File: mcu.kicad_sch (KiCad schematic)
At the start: 30 parts, among them J1 10118193-0001LF, U1 RP2040, U2 AP2112K-3.3TRG1, U3 W25Q16JVSSIQ, Y3 12MHZ

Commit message: Use 402 footprint for rp2040 mcu part
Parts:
- C10, C12, C13, C14, C15, C17, C18, C19, C20, C21, C22, C23, C24, C25: footprint Capacitor_SMD:C_0603_1608Metric_Pad1.08x0.95mm_HandSolder -> Capacitor_SMD:C_0402_1005Metric
- R4, R5, R6, R7, R8, R9: footprint Resistor_SMD:R_0603_1608Metric_Pad0.98x0.95mm_HandSolder -> Resistor_SMD:R_0402_1005Metric
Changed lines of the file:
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@@
       (effects (font (size 1.27 1.27)) (justify left))
     )
-    (property "Footprint" "Capacitor_SMD:C_0603_1608Metric_Pad1.08x0.95mm_HandSolder" (at 187.6552 96.52 0)
+    (property "Footprint" "Capacitor_SMD:C_0402_1005Metric" (at 187.6552 96.52 0)
       (effects (font (size 1.27 1.27)) hide)
     )
@@
       (effects (font (size 1.27 1.27)) (justify left))
     )
-    (property "Footprint" "Capacitor_SMD:C_0603_1608Metric_Pad1.08x0.95mm_HandSolder" (at 221.9452 96.52 0)
+    (property "Footprint" "Capacitor_SMD:C_0402_1005Metric" (at 221.9452 96.52 0)
       (effects (font (size 1.27 1.27)) hide)
     )
@@
       (effects (font (size 1.27 1.27)) (justify left))
     )
-    (property "Footprint" "Capacitor_SMD:C_0603_1608Metric_Pad1.08x0.95mm_HandSolder" (at 275.2852 96.52 0)
+    (property "Footprint" "Capacitor_SMD:C_0402_1005Metric" (at 275.2852 96.52 0)
       (effects (font (size 1.27 1.27)) hide)
     )
@@
       (effects (font (size 1.27 1.27)))
     )
-    (property "Footprint" "Resistor_SMD:R_0603_1608Metric_Pad0.98x0.95mm_HandSolder" (at 198.12 125.222 90)
+    (property "Footprint" "Resistor_SMD:R_0402_1005Metric" (at 198.12 125.222 90)
       (effects (font (size 1.27 1.27)) hide)
     )
@@
       (effects (font (size 1.27 1.27)) (justify left))
     )
-    (property "Footprint" "Capacitor_SMD:C_0603_1608Metric_Pad1.08x0.95mm_HandSolder" (at 263.8552 96.52 0)
+    (property "Footprint" "Capacitor_SMD:C_0402_1005Metric" (at 263.8552 96.52 0)
       (effects (font (size 1.27 1.27)) hide)
     )
@@
       (effects (font (size 1.27 1.27)))
     )
-    (property "Footprint" "Resistor_SMD:R_0603_1608Metric_Pad0.98x0.95mm_HandSolder" (at 158.75 151.892 90)
+    (property "Footprint" "Resistor_SMD:R_0402_1005Metric" (at 158.75 151.892 90)
       (effects (font (size 1.27 1.27)) hide)
     )
@@
       (effects (font (size 1.27 1.27)) (justify left))
     )
-    (property "Footprint" "Capacitor_SMD:C_0603_1608Metric_Pad1.08x0.95mm_HandSolder" (at 199.0852 96.52 0)
+    (property "Footprint" "Capacitor_SMD:C_0402_1005Metric" (at 199.0852 96.52 0)
       (effects (font (size 1.27 1.27)) hide)
     )
@@
       (effects (font (size 1.27 1.27)) (justify left))
     )
-    (property "Footprint" "Capacitor_SMD:C_0603_1608Metric_Pad1.08x0.95mm_HandSolder" (at 168.6052 173.99 0)
+    (property "Footprint" "Capacitor_SMD:C_0402_1005Metric" (at 168.6052 173.99 0)
       (effects (font (size 1.27 1.27)) hide)
     )
@@
       (effects (font (size 1.27 1.27)) (justify left))
     )
-    (property "Footprint" "Capacitor_SMD:C_0603_1608Metric_Pad1.08x0.95mm_HandSolder" (at 150.8252 173.99 0)
+    (property "Footprint" "Capacitor_SMD:C_0402_1005Metric" (at 150.8252 173.99 0)
       (effects (font (size 1.27 1.27)) hide)
     )
@@
       (effects (font (size 1.27 1.27)) (justify left))
     )
-    (property "Footprint" "Capacitor_SMD:C_0603_1608Metric_Pad1.08x0.95mm_HandSolder" (at 154.6352 73.66 0)
+    (property "Footprint" "Capacitor_SMD:C_0402_1005Metric" (at 154.6352 73.66 0)
       (effects (font (size 1.27 1.27)) hide)
     )
@@
       (effects (font (size 1.27 1.27)) (justify left))
     )
-    (property "Footprint" "Capacitor_SMD:C_0603_1608Metric_Pad1.08x0.95mm_HandSolder" (at 244.8052 96.52 0)
+    (property "Footprint" "Capacitor_SMD:C_0402_1005Metric" (at 244.8052 96.52 0)
       (effects (font (size 1.27 1.27)) hide)
     )
@@
       (effects (font (size 1.27 1.27)))
     )
-    (property "Footprint" "Resistor_SMD:R_0603_1608Metric_Pad0.98x0.95mm_HandSolder" (at 128.27 132.842 90)
+    (property "Footprint" "Resistor_SMD:R_0402_1005Metric" (at 128.27 132.842 90)
       (effects (font (size 1.27 1.27)) hide)
     )
@@
       (effects (font (size 1.27 1.27)) (justify left))
     )
-    (property "Footprint" "Capacitor_SMD:C_0603_1608Metric_Pad1.08x0.95mm_HandSolder" (at 135.5852 162.56 0)
+    (property "Footprint" "Capacitor_SMD:C_0402_1005Metric" (at 135.5852 162.56 0)
       (effects (font (size 1.27 1.27)) hide)
     )
@@
       (effects (font (size 1.27 1.27)) (justify left))
     )
-    (property "Footprint" "Resistor_SMD:R_0603_1608Metric_Pad0.98x0.95mm_HandSolder" (at 165.862 160.02 90)
+    (property "Footprint" "Resistor_SMD:R_0402_1005Metric" (at 165.862 160.02 90)
       (effects (font (size 1.27 1.27)) hide)
     )
@@
       (effects (font (size 1.27 1.27)) (justify left))
     )
-    (property "Footprint" "Resistor_SMD:R_0603_1608Metric_Pad0.98x0.95mm_HandSolder" (at 202.692 120.65 90)
+    (property "Footprint" "Resistor_SMD:R_0402_1005Metric" (at 202.692 120.65 90)
       (effects (font (size 1.27 1.27)) hide)
     )
@@
       (effects (font (size 1.27 1.27)))
     )
-    (property "Footprint" "Resistor_SMD:R_0603_1608Metric_Pad0.98x0.95mm_HandSolder" (at 128.27 140.462 90)
+    (property "Footprint" "Resistor_SMD:R_0402_1005Metric" (at 128.27 140.462 90)
       (effects (font (size 1.27 1.27)) hide)
     )
@@
       (effects (font (size 1.27 1.27)) (justify left))
     )
-    (property "Footprint" "Capacitor_SMD:C_0603_1608Metric_Pad1.08x0.95mm_HandSolder" (at 125.4252 162.56 0)
+    (property "Footprint" "Capacitor_SMD:C_0402_1005Metric" (at 125.4252 162.56 0)
       (effects (font (size 1.27 1.27)) hide)
     )
@@
       (effects (font (size 1.27 1.27)) (justify left))
     )
-    (property "Footprint" "Capacitor_SMD:C_0603_1608Metric_Pad1.08x0.95mm_HandSolder" (at 176.2252 96.52 0)
+    (property "Footprint" "Capacitor_SMD:C_0402_1005Metric" (at 176.2252 96.52 0)
       (effects (font (size 1.27 1.27)) hide)
     )
@@
       (effects (font (size 1.27 1.27)) (justify left))
     )
-    (property "Footprint" "Capacitor_SMD:C_0603_1608Metric_Pad1.08x0.95mm_HandSolder" (at 210.5152 96.52 0)
+    (property "Footprint" "Capacitor_SMD:C_0402_1005Metric" (at 210.5152 96.52 0)
       (effects (font (size 1.27 1.27)) hide)
     )
@@
       (effects (font (size 1.27 1.27)) (justify left))
     )
-    (property "Footprint" "Capacitor_SMD:C_0603_1608Metric_Pad1.08x0.95mm_HandSolder" (at 233.3752 96.52 0)
-      (effects (font (size 1.27 1.27)) hide)
-    )
+    (property "Footprint" "Capacitor_SMD:C_0402_1005Metric" (at 233.3752 96.52 0)
+      (effects (font (size 1.27 1.27)) hide)
+    )

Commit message: Update design
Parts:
- C16: footprint Capacitor_SMD:C_0603_1608Metric_Pad1.08x0.95mm_HandSolder -> Capacitor_SMD:C_0402_1005Metric
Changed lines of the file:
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@@
       (effects (font (size 1.27 1.27)) (justify left))
     )
-    (property "Footprint" "Capacitor_SMD:C_0603_1608Metric_Pad1.08x0.95mm_HandSolder" (at 267.6652 134.62 0)
+    (property "Footprint" "Capacitor_SMD:C_0402_1005Metric" (at 267.6652 134.62 0)
       (effects (font (size 1.27 1.27)) hide)
     )

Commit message: Update design
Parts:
- added J5: Conn_ARM_SWD_TagConnect_TC2030, Connector:Tag-Connect_TC2030-IDC-NL_2x03_P1.27mm_Vertical, symbol Connector:Conn_ARM_SWD_TagConnect_TC2030
- added LED1: 150060VS75000, LED_SMD:LED_0603_1608Metric, symbol rpi-pico-debugger-shoe-rescue:150060VS75000-150060VS75000
- added R2: 1K, Resistor_SMD:R_0402_1005Metric, symbol Device:R
- added SW1: SW_Push, Button_Switch_SMD:SW_SPST_B3U-1000P, symbol Switch:SW_Push
- R1: footprint Resistor_SMD:R_0603_1608Metric_Pad0.98x0.95mm_HandSolder -> Resistor_SMD:R_0402_1005Metric
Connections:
- net +3V3: now also J5.1 (VCC)
- net GND: now also J5.5 (GND), LED1.1 (K), SW1.2
- net GPIO25: now also R2.1
- net SWCLK: now also J5.4 (SWCLK)
- net SWDIO: now also J5.2 (SWDIO)
- net USB_BOOT: now also SW1.1
- net VSYS renamed +5V
- new net: LED1.2 (A), R2.2
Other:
- note added: "BOOTSEL"

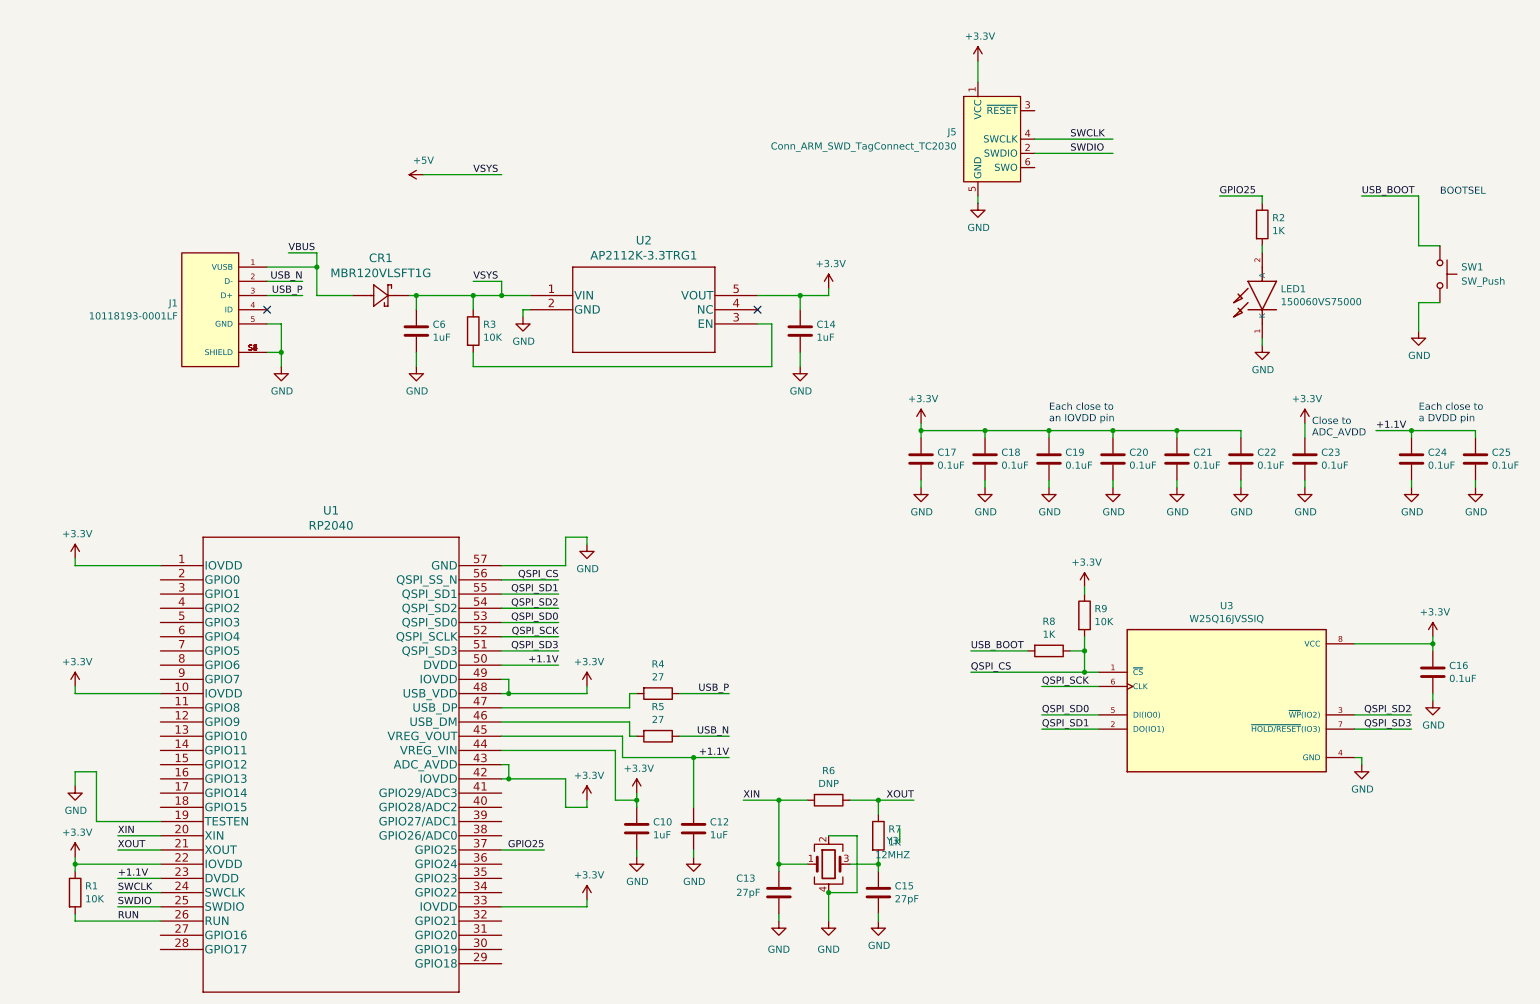
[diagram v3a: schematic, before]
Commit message: Update design place rgb led
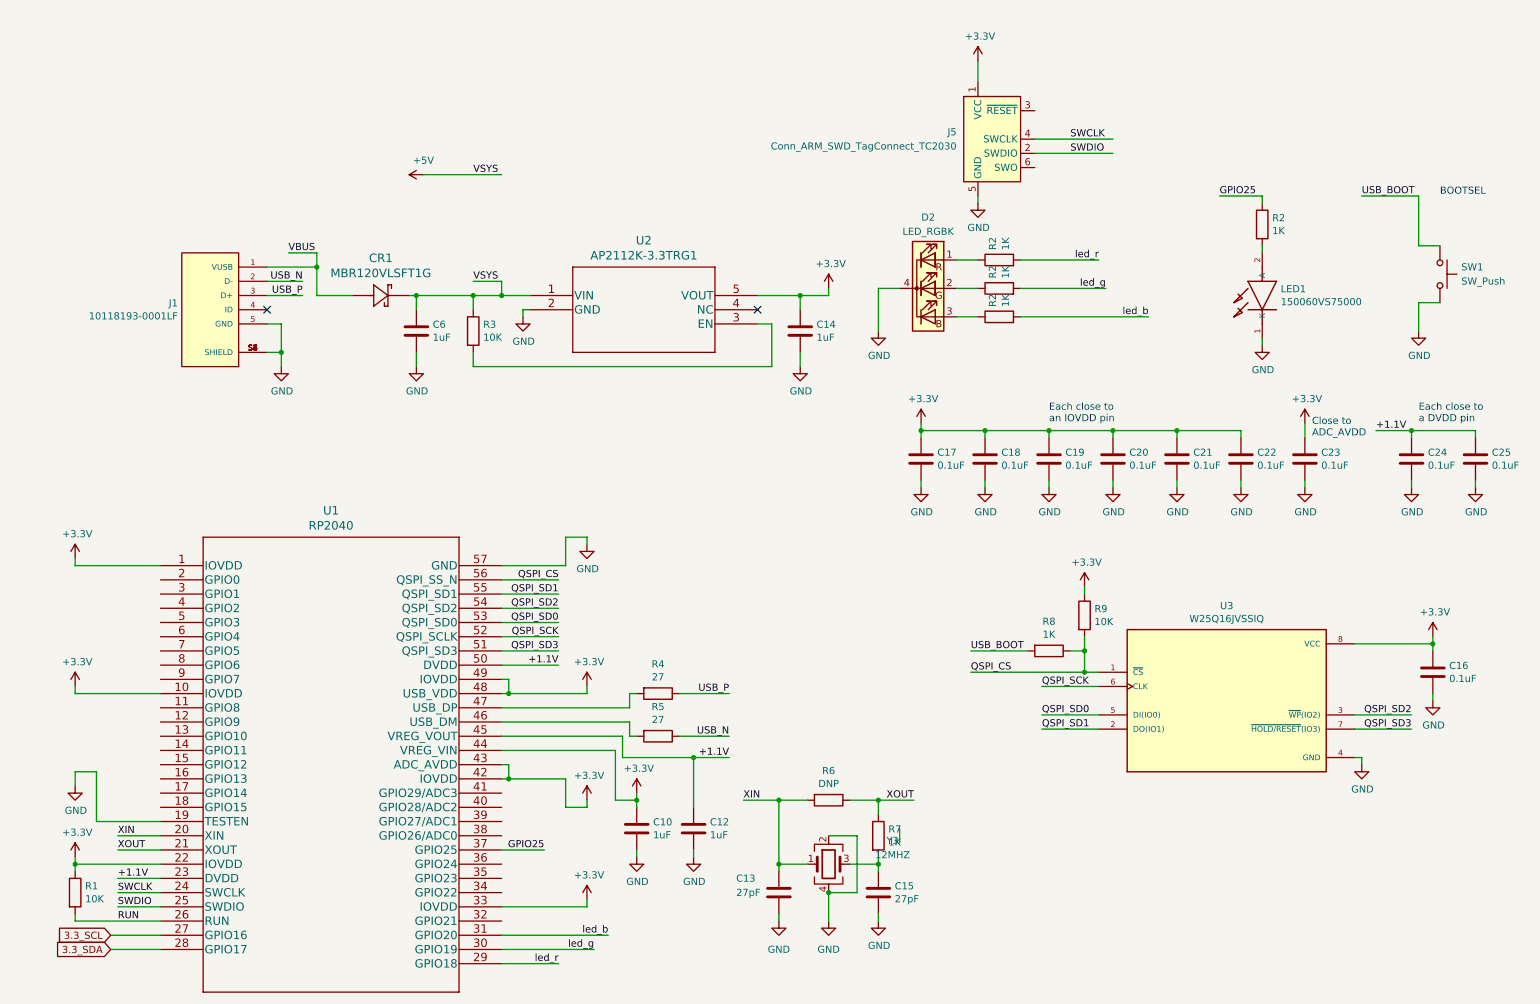
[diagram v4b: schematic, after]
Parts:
- added D2: LED_RGBK, LED_SMD:LED_Lumex_SML-LX0303SIUPGUSB, symbol Device:LED_RGBK
- added R2 (x3): 1K, Resistor_SMD:R_0402_1005Metric, symbol Device:R
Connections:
- net GND: now also D2.4 (K)
- net 3.3_SCL: now reaches U1.27 (GPIO16)
- net 3.3_SDA: now reaches U1.28 (GPIO17)
- net led_r: now reaches U1.29 (GPIO18)
- net led_r: now also R2.2
- net led_g: now reaches U1.30 (GPIO19)
- net led_g: now also R2.2
- net led_b: now reaches U1.31 (GPIO20)
- net led_b: now also R2.2
- new net: D2.1 (RA), R2.1
- new net: D2.2 (GA), R2.1
- new net: D2.3 (BA), R2.1

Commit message: Update design
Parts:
- added D3: LED_RGBK, LED_SMD:LED_Lumex_SML-LX0303SIUPGUSB, symbol Device:LED_RGBK
- added R2 (x3): 1K, Resistor_SMD:R_0402_1005Metric, symbol Device:R
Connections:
- net GND: now also D3.4 (K)
- net led_0_r: now reaches U1.32 (GPIO21)
- net led_0_r: now also R2.2
- net led_0_g: now reaches U1.34 (GPIO22)
- net led_0_g: now also R2.2
- net led_0_b: now reaches U1.35 (GPIO23)
- net led_0_b: now also R2.2
- new net: D3.1 (RA), R2.1
- new net: D3.2 (GA), R2.1
- new net: D3.3 (BA), R2.1
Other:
- moved on the sheet: J5

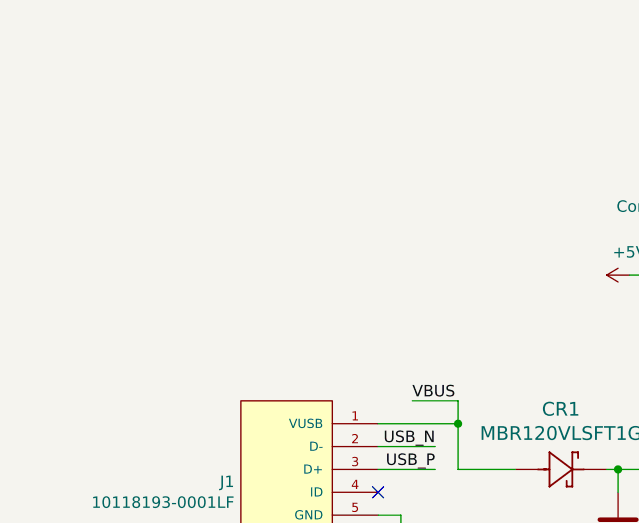
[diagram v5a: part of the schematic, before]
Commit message: Add user buttons
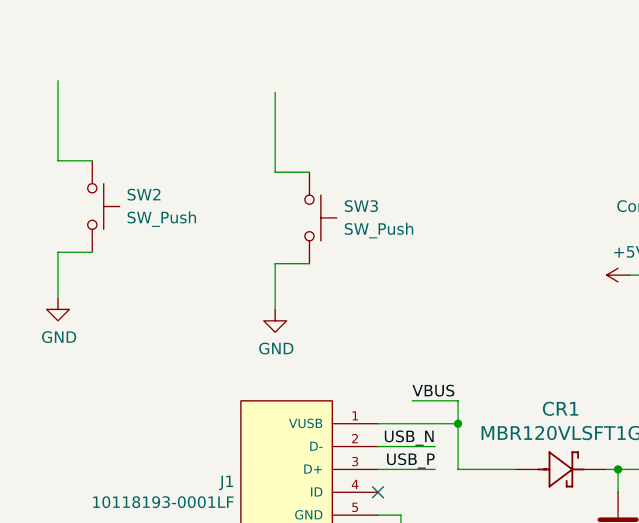
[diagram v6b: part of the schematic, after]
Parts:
- added SW2, SW3: SW_Push, Button_Switch_SMD:SW_SPST_B3U-1000P, symbol Switch:SW_Push
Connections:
- net GND: now also SW2.2, SW3.2
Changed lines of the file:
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@@
+    (stroke (width 0) (type default))
+  )
+  (wire (pts (xy 22.86 39.37) (xy 26.67 39.37))
     (stroke (width 0) (type default))
   )
@@
     (stroke (width 0) (type default))
   )
+  (wire (pts (xy 22.86 39.37) (xy 22.86 44.45))
+    (stroke (width 0) (type default))
+  )
   (wire (pts (xy 232.41 88.9) (xy 232.41 87.63))
     (stroke (width 0) (type default))
@@
     (stroke (width 0) (type default))
   )
+  (wire (pts (xy 46.99 21.59) (xy 46.99 30.48))
+    (stroke (width 0) (type default))
+  )
   (wire (pts (xy 85.09 73.66) (xy 85.09 76.2))
     (stroke (width 0) (type default))
@@
     (stroke (width 0) (type default))
   )
+  (wire (pts (xy 46.99 40.64) (xy 46.99 45.72))
+    (stroke (width 0) (type default))
+  )
   (wire (pts (xy 100.33 116.84) (xy 110.49 116.84))
     (stroke (width 0) (type default))
@@
     (stroke (width 0) (type default))
   )
+  (wire (pts (xy 22.86 20.32) (xy 22.86 29.21))
+    (stroke (width 0) (type default))
+  )
   (wire (pts (xy 39.37 167.64) (xy 31.75 167.64))
     (stroke (width 0) (type default))
@@
     (stroke (width 0) (type default))
   )
+  (wire (pts (xy 46.99 30.48) (xy 50.8 30.48))
+    (stroke (width 0) (type default))
+  )
   (wire (pts (xy 101.6 149.86) (xy 111.76 149.86))
     (stroke (width 0) (type default))
@@
     (stroke (width 0) (type default))
   )
+  (wire (pts (xy 46.99 40.64) (xy 50.8 40.64))
+    (stroke (width 0) (type default))
+  )
   (wire (pts (xy 243.84 96.52) (xy 243.84 97.79))
     (stroke (width 0) (type default))
@@
   )
   (wire (pts (xy 100.33 167.64) (xy 120.65 167.64))
+    (stroke (width 0) (type default))
+  )
+  (wire (pts (xy 22.86 29.21) (xy 26.67 29.21))
     (stroke (width 0) (type default))
   )
@@
     )
   )
+  (symbol (lib_id "Switch:SW_Push") (at 26.67 34.29 270) (unit 1)
+    (in_bom yes) (on_board yes) (dnp no) (fields_autoplaced)
+    (property "Reference" "SW2" (at 30.48 33.02 90)
+      (effects (font (size 1.27 1.27)) (justify left))
+    )
+    (property "Value" "SW_Push" (at 30.48 35.56 90)
+      (effects (font (size 1.27 1.27)) (justify left))
+    )
+    (property "Footprint" "Button_Switch_SMD:SW_SPST_B3U-1000P" (at 31.75 34.29 0)
+      (effects (font (size 1.27 1.27)) hide)
+    )
+    (property "Datasheet" "~" (at 31.75 34.29 0)
+      (effects (font (size 1.27 1.27)) hide)
+    )
+    (pin "1")
+    (pin "2")
+    (instances
+      (project "ltp_kikad"
+        (path "/eed35b77-cbf9-4596-9b17-2558f81058ba/643f5372-7b7f-4a0a-9eb8-fe959bdc465c"
+          (reference "SW2") (unit 1)
+        )
+      )
+    )
+  )
   (symbol (lib_id "power:GND") (at 104.14 67.31 0) (unit 1)
     (in_bom yes) (on_board yes) (dnp no)
@@
         (path "/eed35b77-cbf9-4596-9b17-2558f81058ba/643f5372-7b7f-4a0a-9eb8-fe959bdc465c"
           (reference "C27") (unit 1)
+        )
+      )
+    )
+  )
+  (symbol (lib_id "power:GND") (at 22.86 44.45 0) (unit 1)
+    (in_bom yes) (on_board yes) (dnp no)
+    (property "Reference" "#PWR0134" (at 22.86 50.8 0)
+      (effects (font (size 1.27 1.27)) hide)
+    )
+    (property "Value" "GND" (at 22.987 48.8442 0)
+      (effects (font (size 1.27 1.27)))
+    )
+    (property "Footprint" "" (at 22.86 44.45 0)
+      (effects (font (size 1.27 1.27)) hide)
+    )
+    (property "Datasheet" "" (at 22.86 44.45 0)
+      (effects (font (size 1.27 1.27)) hide)
+    )
+    (pin "1")
+    (instances
+      (project "rpi-pico-debugger-shoe"
+        (path "/aad74d97-f116-4a83-b498-c8cb2f4b4e35"
+          (reference "#PWR0134") (unit 1)
+        )
+      )
+      (project "ltp_kikad"
+        (path "/eed35b77-cbf9-4596-9b17-2558f81058ba/643f5372-7b7f-4a0a-9eb8-fe959bdc465c"
+          (reference "#PWR063") (unit 1)
         )
       )
@@
         (path "/eed35b77-cbf9-4596-9b17-2558f81058ba/643f5372-7b7f-4a0a-9eb8-fe959bdc465c"
           (reference "#PWR083") (unit 1)
+        )
+      )
+    )
+  )
+  (symbol (lib_id "Switch:SW_Push") (at 50.8 35.56 270) (unit 1)
+    (in_bom yes) (on_board yes) (dnp no) (fields_autoplaced)
+    (property "Reference" "SW3" (at 54.61 34.29 90)
+      (effects (font (size 1.27 1.27)) (justify left))
+    )
+    (property "Value" "SW_Push" (at 54.61 36.83 90)
+      (effects (font (size 1.27 1.27)) (justify left))
+    )
+    (property "Footprint" "Button_Switch_SMD:SW_SPST_B3U-1000P" (at 55.88 35.56 0)
+      (effects (font (size 1.27 1.27)) hide)
+    )
+    (property "Datasheet" "~" (at 55.88 35.56 0)
+      (effects (font (size 1.27 1.27)) hide)
+    )
+    (pin "1")
+    (pin "2")
+    (instances
+      (project "ltp_kikad"
+        (path "/eed35b77-cbf9-4596-9b17-2558f81058ba/643f5372-7b7f-4a0a-9eb8-fe959bdc465c"
+          (reference "SW3") (unit 1)
         )
       )
@@
         )
       )
+    )
+  )
+  (symbol (lib_id "power:GND") (at 46.99 45.72 0) (unit 1)
+    (in_bom yes) (on_board yes) (dnp no)
+    (property "Reference" "#PWR0134" (at 46.99 52.07 0)
+      (effects (font (size 1.27 1.27)) hide)
+    )
+    (property "Value" "GND" (at 47.117 50.1142 0)
+      (effects (font (size 1.27 1.27)))
+    )
+    (property "Footprint" "" (at 46.99 45.72 0)
+      (effects (font (size 1.27 1.27)) hide)
+    )
+    (property "Datasheet" "" (at 46.99 45.72 0)
+      (effects (font (size 1.27 1.27)) hide)
+    )
+    (pin "1")
+    (instances
+      (project "rpi-pico-debugger-shoe"
+        (path "/aad74d97-f116-4a83-b498-c8cb2f4b4e35"
+          (reference "#PWR0134") (unit 1)
+        )
+      )
+      (project "ltp_kikad"
+        (path "/eed35b77-cbf9-4596-9b17-2558f81058ba/643f5372-7b7f-4a0a-9eb8-fe959bdc465c"
+          (reference "#PWR064") (unit 1)
+        )
+      )
